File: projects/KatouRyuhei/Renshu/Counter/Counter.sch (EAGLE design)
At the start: 10 parts

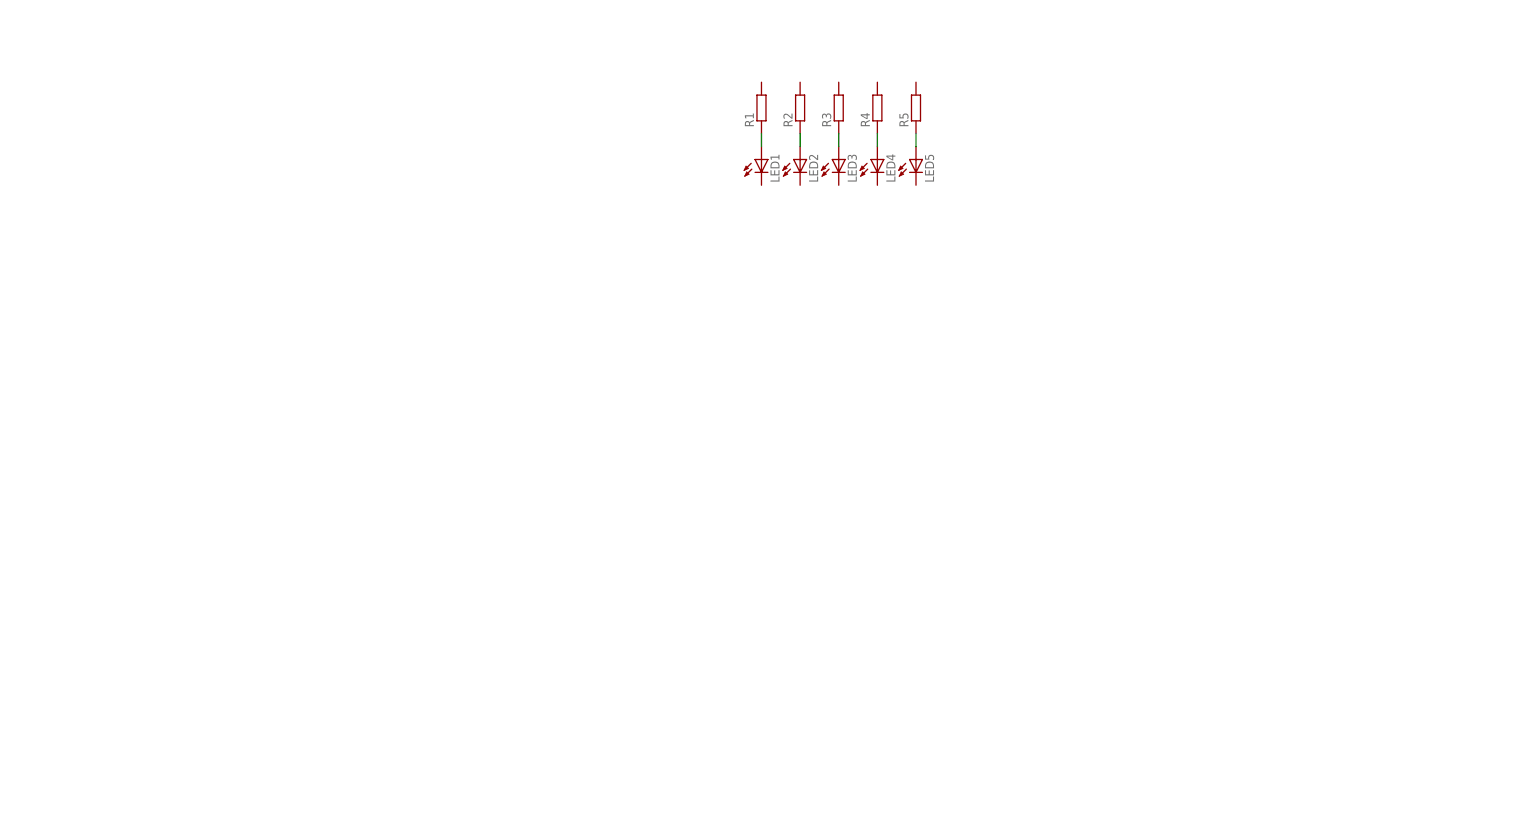
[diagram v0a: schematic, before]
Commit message: 2桁10進数カウンタ
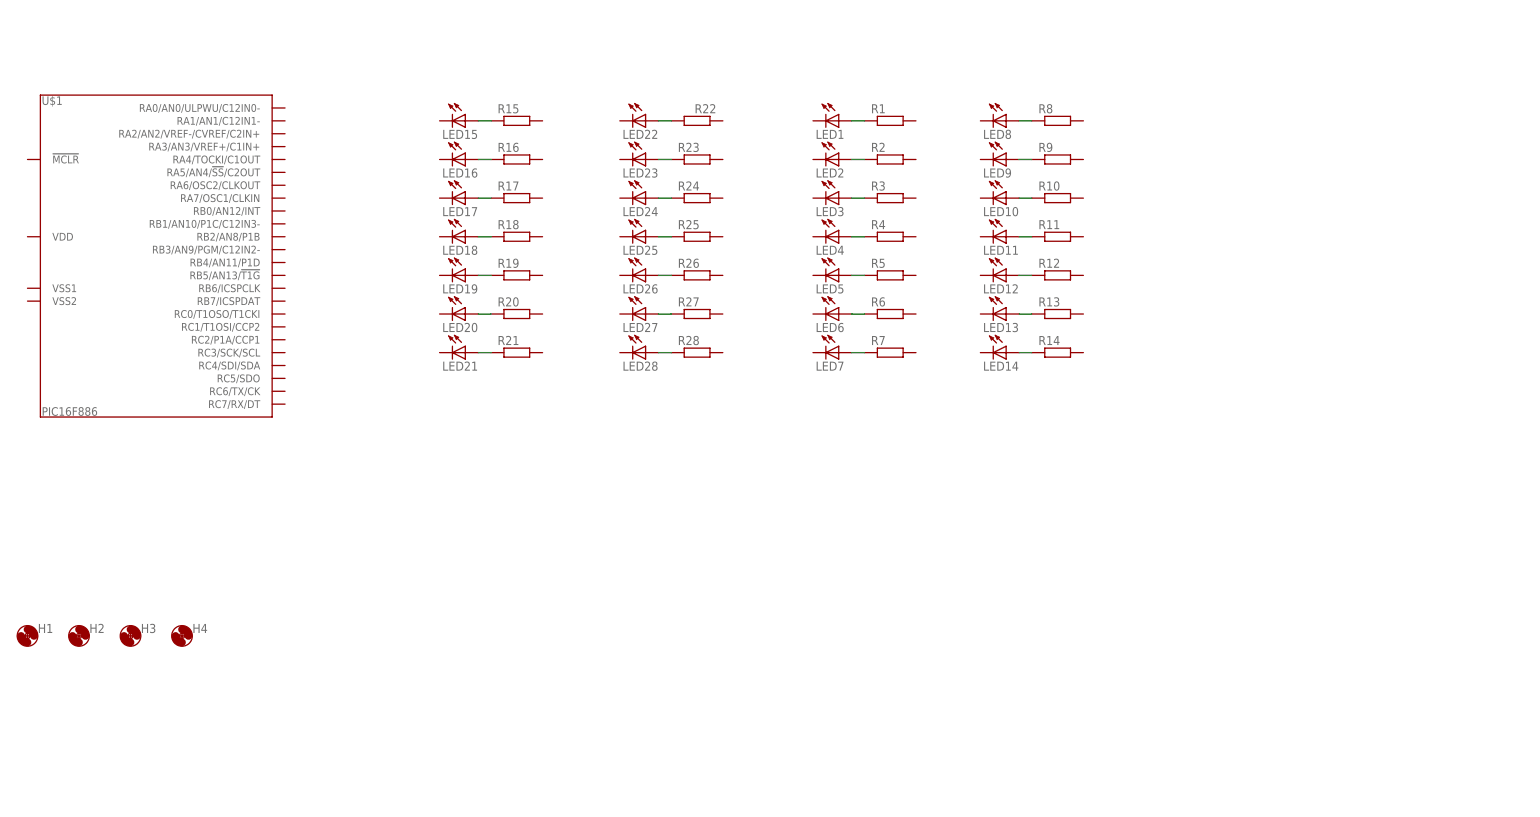
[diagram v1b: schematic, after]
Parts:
- added H1, H2, H3, H4: HOLE3.3M3BOLT, Hole:HOLE3.3M3BOLT
- added LED10, LED11, LED12, LED13, LED14, LED15, LED16, LED17, LED18, LED19, LED20, LED21, LED22, LED23, LED24, LED25, LED26, LED27, LED28, LED6, LED7, LED8, LED9: (no value), FP-21T for MITS:LED5MM
- added R10, R11, R12, R13, R14, R15, R16, R17, R18, R19, R20, R21, R22, R23, R24, R25, R26, R27, R28, R6, R7, R8, R9: (no value), rcl:R-EU_R3216W
- added U$1: PIC16F886, PIC:PIC16F886
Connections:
- new net N$10: LED10.A, R10.1
- new net N$11: LED11.A, R11.1
- new net N$12: LED12.A, R12.1
- new net N$13: LED13.A, R13.1
- new net N$14: LED14.A, R14.1
- new net N$15: LED15.A, R15.1
- new net N$16: LED16.A, R16.1
- new net N$17: LED17.A, R17.1
- new net N$18: LED18.A, R18.1
- new net N$19: LED19.A, R19.1
- new net N$20: LED20.A, R20.1
- new net N$21: LED21.A, R21.1
- new net N$22: LED22.A, R22.2
- new net N$23: LED23.A, R23.1
- new net N$24: LED24.A, R24.1
- new net N$25: LED25.A, R25.1
- new net N$26: LED26.A, R26.1
- new net N$27: LED27.A, R27.1
- new net N$28: LED28.A, R28.1
- new net N$6: LED6.A, R6.1
- new net N$7: LED7.A, R7.1
- new net N$8: LED8.A, R8.1
- new net N$9: LED9.A, R9.1
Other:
- moved on the sheet: LED1, LED2, LED3, LED4, LED5, R1, R2, R3, R4, R5

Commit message: 10進数2桁カウンタ作成途中
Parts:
- added S1: (no value), switch:SLIDESW
- added U$2: PIC16F886, PIC:PIC16F886
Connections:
- new net GND: U$1.VSS1, U$1.VSS2, U$2.VSS1, U$2.VSS2
- new net VDD: U$1.VDD, U$2.VDD
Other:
- moved on the sheet: H1, H2, H3, H4, U$1
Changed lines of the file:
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@@
 <layer number="51" name="tDocu" color="6" fill="1" visible="no" active="no"/>
 <layer number="52" name="bDocu" color="7" fill="1" visible="no" active="no"/>
+<layer number="53" name="tGND_GNDA" color="7" fill="9" visible="no" active="no"/>
+<layer number="54" name="bGND_GNDA" color="1" fill="9" visible="no" active="no"/>
 <layer number="91" name="Nets" color="2" fill="1" visible="yes" active="yes"/>
 <layer number="92" name="Busses" color="1" fill="1" visible="yes" active="yes"/>
@@
 <part name="H3" library="Hole" deviceset="HOLE3.3" device="M3BOLT"/>
 <part name="H4" library="Hole" deviceset="HOLE3.3" device="M3BOLT"/>
+<part name="VDD1" library="supply1" deviceset="VDD" device=""/>
+<part name="GND1" library="supply1" deviceset="GND" device=""/>
+<part name="GND2" library="supply1" deviceset="GND" device=""/>
+<part name="S1" library="switch" deviceset="SLIDESW" device=""/>
+<part name="U$2" library="PIC" deviceset="PIC16F886" device=""/>
+<part name="VDD2" library="supply1" deviceset="VDD" device=""/>
+<part name="GND3" library="supply1" deviceset="GND" device=""/>
+<part name="GND4" library="supply1" deviceset="GND" device=""/>
 </parts>
 <sheets>
@@
 <instance part="LED27" gate="G$1" x="-96.52" y="88.9" rot="R270"/>
 <instance part="LED28" gate="G$1" x="-96.52" y="81.28" rot="R270"/>
-<instance part="U$1" gate="IC" x="-193.04" y="99.06"/>
-<instance part="H1" gate="G$1" x="-218.44" y="25.4"/>
-<instance part="H2" gate="G$1" x="-208.28" y="25.4"/>
-<instance part="H3" gate="G$1" x="-198.12" y="25.4"/>
-<instance part="H4" gate="G$1" x="-187.96" y="25.4"/>
+<instance part="U$1" gate="IC" x="-187.96" y="99.06"/>
+<instance part="H1" gate="G$1" x="-121.92" y="15.24"/>
+<instance part="H2" gate="G$1" x="-111.76" y="15.24"/>
+<instance part="H3" gate="G$1" x="-101.6" y="15.24"/>
+<instance part="H4" gate="G$1" x="-91.44" y="15.24"/>
+<instance part="VDD1" gate="G$1" x="-215.9" y="104.14" rot="R90"/>
+<instance part="GND1" gate="1" x="-218.44" y="93.98" rot="R270"/>
+<instance part="GND2" gate="1" x="-215.9" y="86.36"/>
+<instance part="S1" gate="1" x="-121.92" y="48.26" rot="R270"/>
+<instance part="U$2" gate="IC" x="-187.96" y="22.86"/>
+<instance part="VDD2" gate="G$1" x="-215.9" y="27.94" rot="R90"/>
+<instance part="GND3" gate="1" x="-218.44" y="17.78" rot="R270"/>
+<instance part="GND4" gate="1" x="-215.9" y="10.16"/>
 </instances>
 <busses>
@@
 </segment>
 </net>
+<net name="VDD" class="0">
+<segment>
+<pinref part="U$1" gate="IC" pin="VDD"/>
+<pinref part="VDD1" gate="G$1" pin="VDD"/>
+</segment>
+<segment>
+<pinref part="U$2" gate="IC" pin="VDD"/>
+<pinref part="VDD2" gate="G$1" pin="VDD"/>
+</segment>
+</net>
+<net name="GND" class="0">
+<segment>
+<pinref part="U$1" gate="IC" pin="VSS1"/>
+<pinref part="GND1" gate="1" pin="GND"/>
+<wire x1="-213.36" y1="93.98" x2="-215.9" y2="93.98" width="0.1524" layer="91"/>
+</segment>
+<segment>
+<pinref part="U$1" gate="IC" pin="VSS2"/>
+<pinref part="GND2" gate="1" pin="GND"/>
+<wire x1="-213.36" y1="91.44" x2="-215.9" y2="91.44" width="0.1524" layer="91"/>
+<wire x1="-215.9" y1="91.44" x2="-215.9" y2="88.9" width="0.1524" layer="91"/>
+</segment>
+<segment>
+<pinref part="U$2" gate="IC" pin="VSS1"/>
+<pinref part="GND3" gate="1" pin="GND"/>
+<wire x1="-213.36" y1="17.78" x2="-215.9" y2="17.78" width="0.1524" layer="91"/>
+</segment>
+<segment>
+<pinref part="U$2" gate="IC" pin="VSS2"/>
+<pinref part="GND4" gate="1" pin="GND"/>
+<wire x1="-213.36" y1="15.24" x2="-215.9" y2="15.24" width="0.1524" layer="91"/>
+<wire x1="-215.9" y1="15.24" x2="-215.9" y2="12.7" width="0.1524" layer="91"/>
+</segment>
+</net>

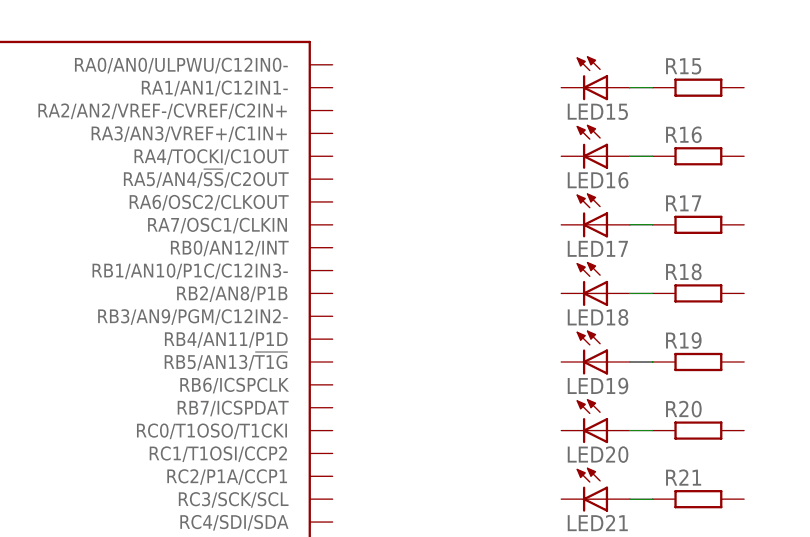
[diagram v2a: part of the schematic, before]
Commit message: 10進数2桁カウンタ製作途中
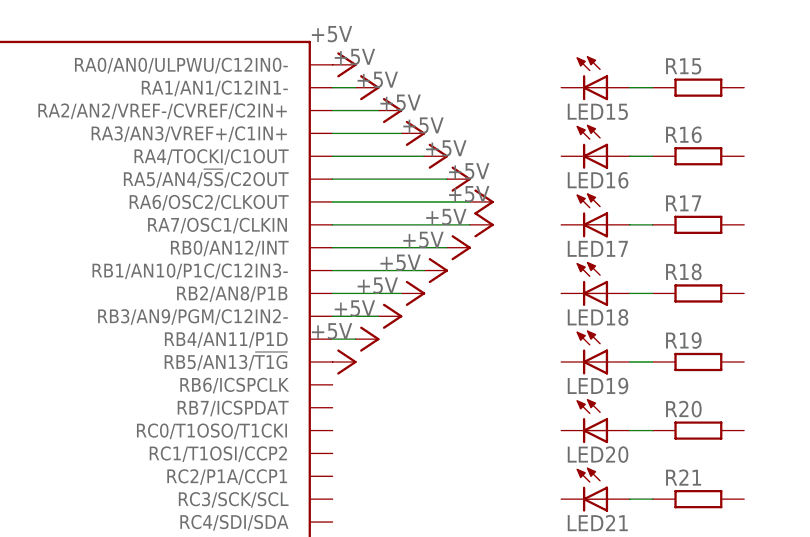
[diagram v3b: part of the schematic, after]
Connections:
- new net +5V: U$1.RA0/AN0/ULPWU/C12IN0-, U$1.RA1/AN1/C12IN1-, U$1.RA2/AN2/VREF-/CVREF/C2IN+, U$1.RA3/AN3/VREF+/C1IN+, U$1.RA4/TOCKI/C1OUT, U$1.RA5/AN4/!SS!/C2OUT, U$1.RA6/OSC2/CLKOUT, U$1.RA7/OSC1/CLKIN, U$1.RB0/AN12/INT, U$1.RB1/AN10/P1C/C12IN3-, U$1.RB2/AN8/P1B, U$1.RB3/AN9/PGM/C12IN2-, U$1.RB4/AN11/P1D, U$1.RB5/AN13/!T1G
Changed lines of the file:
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@@
 <part name="GND3" library="supply1" deviceset="GND" device=""/>
 <part name="GND4" library="supply1" deviceset="GND" device=""/>
+<part name="P+1" library="supply1" deviceset="+5V" device=""/>
+<part name="P+2" library="supply1" deviceset="+5V" device=""/>
+<part name="P+3" library="supply1" deviceset="+5V" device=""/>
+<part name="P+4" library="supply1" deviceset="+5V" device=""/>
+<part name="P+5" library="supply1" deviceset="+5V" device=""/>
+<part name="P+6" library="supply1" deviceset="+5V" device=""/>
+<part name="P+7" library="supply1" deviceset="+5V" device=""/>
+<part name="P+8" library="supply1" deviceset="+5V" device=""/>
+<part name="P+9" library="supply1" deviceset="+5V" device=""/>
+<part name="P+10" library="supply1" deviceset="+5V" device=""/>
+<part name="P+11" library="supply1" deviceset="+5V" device=""/>
+<part name="P+12" library="supply1" deviceset="+5V" device=""/>
+<part name="P+13" library="supply1" deviceset="+5V" device=""/>
+<part name="P+14" library="supply1" deviceset="+5V" device=""/>
 </parts>
 <sheets>
@@
 <instance part="GND3" gate="1" x="-218.44" y="17.78" rot="R270"/>
 <instance part="GND4" gate="1" x="-215.9" y="10.16"/>
+<instance part="P+1" gate="1" x="-160.02" y="129.54" rot="R270"/>
+<instance part="P+2" gate="1" x="-157.48" y="127" rot="R270"/>
+<instance part="P+3" gate="1" x="-154.94" y="124.46" rot="R270"/>
+<instance part="P+4" gate="1" x="-152.4" y="121.92" rot="R270"/>
+<instance part="P+5" gate="1" x="-149.86" y="119.38" rot="R270"/>
+<instance part="P+6" gate="1" x="-147.32" y="116.84" rot="R270"/>
+<instance part="P+7" gate="1" x="-144.78" y="114.3" rot="R270"/>
+<instance part="P+8" gate="1" x="-144.78" y="111.76" rot="R270"/>
+<instance part="P+9" gate="1" x="-147.32" y="109.22" rot="R270"/>
+<instance part="P+10" gate="1" x="-149.86" y="106.68" rot="R270"/>
+<instance part="P+11" gate="1" x="-152.4" y="104.14" rot="R270"/>
+<instance part="P+12" gate="1" x="-154.94" y="101.6" rot="R270"/>
+<instance part="P+13" gate="1" x="-157.48" y="99.06" rot="R270"/>
+<instance part="P+14" gate="1" x="-160.02" y="96.52" rot="R270"/>
 </instances>
 <busses>
@@
 </segment>
 </net>
+<net name="+5V" class="0">
+<segment>
+<pinref part="U$1" gate="IC" pin="RA0/AN0/ULPWU/C12IN0-"/>
+<pinref part="P+1" gate="1" pin="+5V"/>
+</segment>
+<segment>
+<pinref part="U$1" gate="IC" pin="RA1/AN1/C12IN1-"/>
+<pinref part="P+2" gate="1" pin="+5V"/>
+<wire x1="-162.56" y1="127" x2="-160.02" y2="127" width="0.1524" layer="91"/>
+</segment>
+<segment>
+<pinref part="U$1" gate="IC" pin="RA2/AN2/VREF-/CVREF/C2IN+"/>
+<pinref part="P+3" gate="1" pin="+5V"/>
+<wire x1="-162.56" y1="124.46" x2="-157.48" y2="124.46" width="0.1524" layer="91"/>
+</segment>
+<segment>
+<pinref part="U$1" gate="IC" pin="RA3/AN3/VREF+/C1IN+"/>
+<pinref part="P+4" gate="1" pin="+5V"/>
+<wire x1="-162.56" y1="121.92" x2="-154.94" y2="121.92" width="0.1524" layer="91"/>
+</segment>
+<segment>
+<pinref part="U$1" gate="IC" pin="RA4/TOCKI/C1OUT"/>
+<pinref part="P+5" gate="1" pin="+5V"/>
+<wire x1="-162.56" y1="119.38" x2="-152.4" y2="119.38" width="0.1524" layer="91"/>
+</segment>
+<segment>
+<pinref part="U$1" gate="IC" pin="RA5/AN4/!SS!/C2OUT"/>
+<pinref part="P+6" gate="1" pin="+5V"/>
+<wire x1="-162.56" y1="116.84" x2="-149.86" y2="116.84" width="0.1524" layer="91"/>
+</segment>
+<segment>
+<pinref part="U$1" gate="IC" pin="RA6/OSC2/CLKOUT"/>
+<pinref part="P+7" gate="1" pin="+5V"/>
+<wire x1="-162.56" y1="114.3" x2="-147.32" y2="114.3" width="0.1524" layer="91"/>
+</segment>
+<segment>
+<pinref part="U$1" gate="IC" pin="RB5/AN13/!T1G"/>
+<pinref part="P+14" gate="1" pin="+5V"/>
+</segment>
+<segment>
+<pinref part="U$1" gate="IC" pin="RB4/AN11/P1D"/>
+<pinref part="P+13" gate="1" pin="+5V"/>
+<wire x1="-162.56" y1="99.06" x2="-160.02" y2="99.06" width="0.1524" layer="91"/>
+</segment>
+<segment>
+<pinref part="U$1" gate="IC" pin="RB3/AN9/PGM/C12IN2-"/>
+<pinref part="P+12" gate="1" pin="+5V"/>
+<wire x1="-162.56" y1="101.6" x2="-157.48" y2="101.6" width="0.1524" layer="91"/>
+</segment>
+<segment>
+<pinref part="U$1" gate="IC" pin="RB2/AN8/P1B"/>
+<pinref part="P+11" gate="1" pin="+5V"/>
+<wire x1="-162.56" y1="104.14" x2="-154.94" y2="104.14" width="0.1524" layer="91"/>
+</segment>
+<segment>
+<pinref part="U$1" gate="IC" pin="RB1/AN10/P1C/C12IN3-"/>
+<pinref part="P+10" gate="1" pin="+5V"/>
+<wire x1="-162.56" y1="106.68" x2="-152.4" y2="106.68" width="0.1524" layer="91"/>
+</segment>
+<segment>
+<pinref part="U$1" gate="IC" pin="RB0/AN12/INT"/>
+<pinref part="P+9" gate="1" pin="+5V"/>
+<wire x1="-162.56" y1="109.22" x2="-149.86" y2="109.22" width="0.1524" layer="91"/>
+</segment>
+<segment>
+<pinref part="U$1" gate="IC" pin="RA7/OSC1/CLKIN"/>
+<pinref part="P+8" gate="1" pin="+5V"/>
+<wire x1="-162.56" y1="111.76" x2="-147.32" y2="111.76" width="0.1524" layer="91"/>
+</segment>
+</net>
